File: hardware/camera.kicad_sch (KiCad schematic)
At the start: 4 parts, among them J1 DF37NC-30DS-0.4V_51_

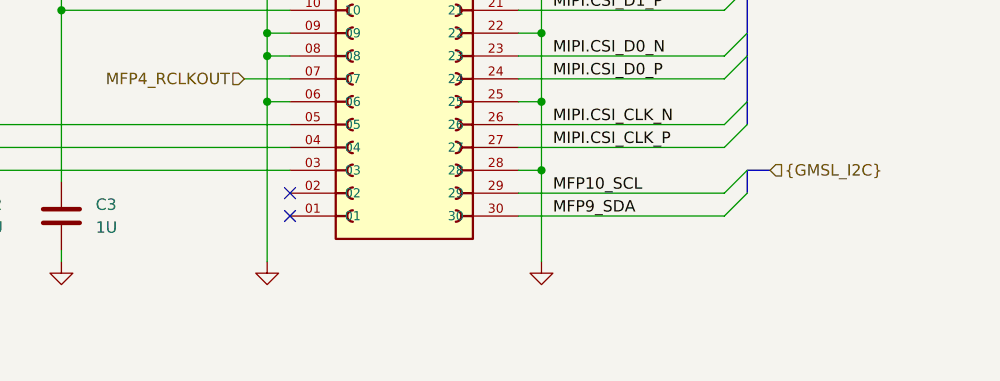
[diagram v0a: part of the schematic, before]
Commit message: finished rough pass on max96717, need cfgs. added notes to imx219 inck tolerance.
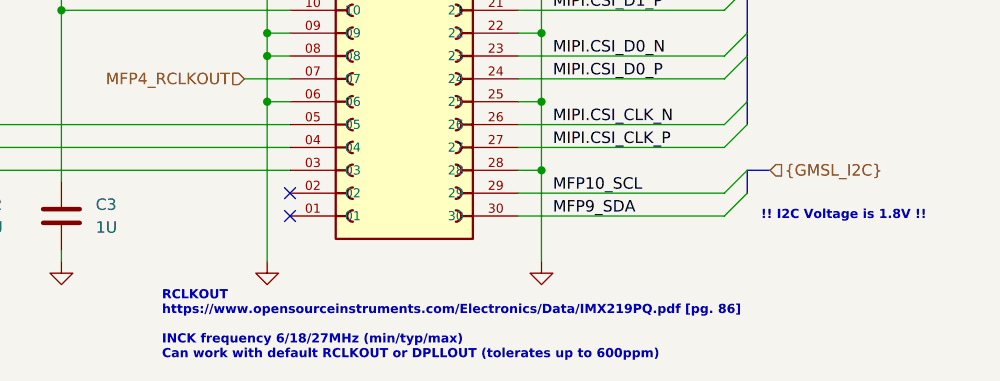
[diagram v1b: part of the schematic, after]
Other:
- note added: "!! I2C Voltage is 1.8V !!"
- note added: "RCLKOUT https://www.opensourceinstruments.com/Electronics/Data/IMX219PQ.pdf [pg. 86] INCK frequency 6/18/27MHz (min/typ/max) Can work with default RCLKOUT or DPLLOUT (tolerates up to 600ppm)"
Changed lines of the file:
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@@
+		)
+	)
+	(text "RCLKOUT\nhttps://www.opensourceinstruments.com/Electronics/Data/IMX219PQ.pdf [pg. 86]\n\nINCK frequency 6/18/27MHz (min/typ/max)\nCan work with default RCLKOUT or DPLLOUT (tolerates up to 600ppm)"
+		(exclude_from_sim no)
+		(at 119.126 126.492 0)
+		(effects
+			(font
+				(size 1.016 1.016)
+				(thickness 0.254)
+				(bold yes)
+				(color 132 132 132 1)
+			)
+			(justify left)
+		)
+	)
+	(text "!! I2C Voltage is 1.8V !!"
+		(exclude_from_sim no)
+		(at 185.674 114.3 0)
+		(effects
+			(font
+				(size 1.016 1.016)
+				(thickness 0.254)
+				(bold yes)
+				(color 255 0 0 1)
+			)
+			(justify left)
 		)
 	)
 	(label "MIPI.CSI_D3_N"
 		(at 115.57 81.28 0)
+		(fields_autoplaced yes)
 		(effects
 			(font
@@
 	(label "MIPI.CSI_D3_P"
 		(at 115.57 83.82 0)
+		(fields_autoplaced yes)
 		(effects
 			(font
@@
 	(label "MIPI.CSI_D0_P"
 		(at 162.56 99.06 0)
+		(fields_autoplaced yes)
 		(effects
 			(font
@@
 	(label "MFP10_SCL"
 		(at 162.56 111.76 0)
+		(fields_autoplaced yes)
 		(effects
 			(font
@@
 	(label "MFP9_SDA"
 		(at 162.56 114.3 0)
+		(fields_autoplaced yes)
 		(effects
 			(font
@@
 	(label "MIPI.CSI_CLK_N"
 		(at 162.56 104.14 0)
+		(fields_autoplaced yes)
 		(effects
 			(font
@@
 	(label "MIPI.CSI_D1_N"
 		(at 162.56 88.9 0)
+		(fields_autoplaced yes)
 		(effects
 			(font
@@
 	(label "MIPI.CSI_D0_N"
 		(at 162.56 96.52 0)
+		(fields_autoplaced yes)
 		(effects
 			(font
@@
 	(label "MIPI.CSI_D1_P"
 		(at 162.56 91.44 0)
+		(fields_autoplaced yes)
 		(effects
 			(font
@@
 	(label "MIPI.CSI_CLK_P"
 		(at 162.56 106.68 0)
+		(fields_autoplaced yes)
 		(effects
 			(font
@@
 	(label "MIPI.CSI_D2_N"
 		(at 162.56 81.28 0)
+		(fields_autoplaced yes)
 		(effects
 			(font
@@
 	(label "MIPI.CSI_D2_P"
 		(at 162.56 83.82 0)
+		(fields_autoplaced yes)
 		(effects
 			(font

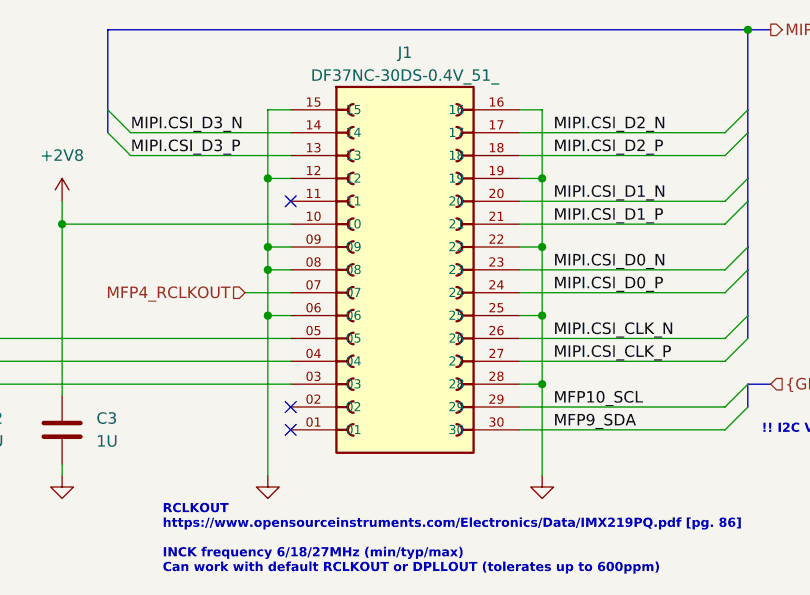
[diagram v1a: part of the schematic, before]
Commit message: Removed DF37 connector
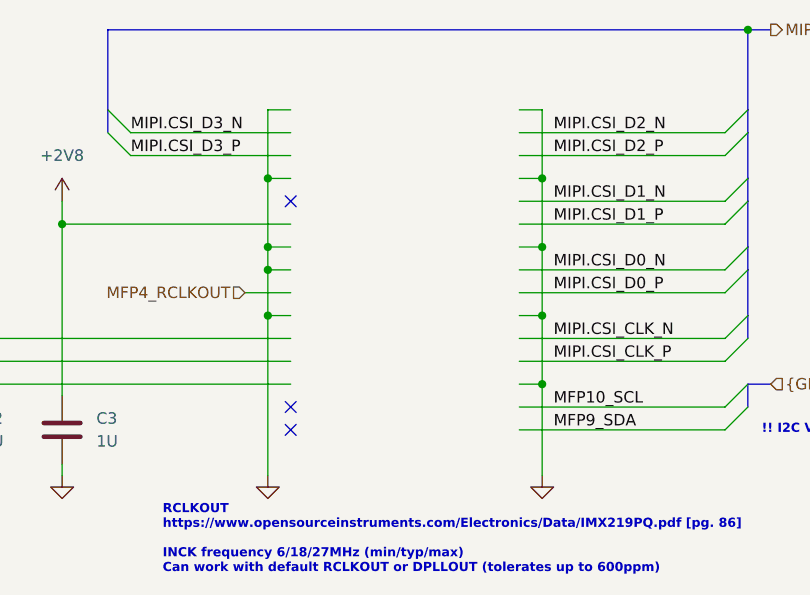
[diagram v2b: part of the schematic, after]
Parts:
- removed J1: DF37NC-30DS-0.4V_51_, user:HRS_DF37NC-30DS-0.4V_51_, symbol user:DF37NC-30DS-0.4V_51_
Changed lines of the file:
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@@
-	)
-	(symbol
-		(lib_id "user:DF37NC-30DS-0.4V_51_")
-		(at 146.05 96.52 0)
-		(unit 1)
-		(exclude_from_sim no)
-		(in_bom yes)
-		(on_board yes)
-		(dnp no)
-		(property "Reference" "J1"
-			(at 146.05 72.39 0)
-			(effects
-				(font
-					(size 1.27 1.27)
-				)
-			)
-		)
-		(property "Value" "DF37NC-30DS-0.4V_51_"
-			(at 146.05 74.93 0)
-			(effects
-				(font
-					(size 1.27 1.27)
-				)
-			)
-		)
-		(property "Footprint" "user:HRS_DF37NC-30DS-0.4V_51_"
-			(at 146.304 128.27 0)
-			(effects
-				(font
-					(size 1.27 1.27)
-				)
-				(justify bottom)
-				(hide yes)
-			)
-		)
-		(property "Datasheet" ""
-			(at 146.05 96.52 0)
-			(effects
-				(font
-					(size 1.27 1.27)
-				)
-				(hide yes)
-			)
-		)
-		(property "Description" ""
-			(at 146.05 96.52 0)
-			(effects
-				(font
-					(size 1.27 1.27)
-				)
-				(hide yes)
-			)
-		)
-		(property "PARTREV" "11.02.09"
-			(at 146.304 125.73 0)
-			(effects
-				(font
-					(size 1.27 1.27)
-				)
-				(justify bottom)
-				(hide yes)
-			)
-		)
-		(property "STANDARD" "Manufacturer Recommendations"
-			(at 146.304 130.556 0)
-			(effects
-				(font
-					(size 1.27 1.27)
-				)
-				(justify bottom)
-				(hide yes)
-			)
-		)
-		(property "MAXIMUM_PACKAGE_HEIGHT" "1.08mm"
-			(at 147.574 133.35 0)
-			(effects
-				(font
-					(size 1.27 1.27)
-				)
-				(justify bottom)
-				(hide yes)
-			)
-		)
-		(property "MANUFACTURER" "Hirose"
-			(at 139.192 133.35 0)
-			(effects
-				(font
-					(size 1.27 1.27)
-				)
-				(justify bottom)
-				(hide yes)
-			)
-		)
-		(pin "25"
-		)
-		(pin "13"
-		)
-		(pin "05"
-		)
-		(pin "17"
-		)
-		(pin "20"
-		)
-		(pin "02"
-		)
-		(pin "12"
-		)
-		(pin "10"
-		)
-		(pin "23"
-		)
-		(pin "14"
-		)
-		(pin "04"
-		)
-		(pin "15"
-		)
-		(pin "27"
-		)
-		(pin "01"
-		)
-		(pin "11"
-		)
-		(pin "21"
-		)
-		(pin "29"
-		)
-		(pin "22"
-		)
-		(pin "24"
-		)
-		(pin "30"
-		)
-		(pin "16"
-		)
-		(pin "19"
-		)
-		(pin "28"
-		)
-		(pin "26"
-		)
-		(pin "09"
-		)
-		(pin "08"
-		)
-		(pin "18"
-		)
-		(pin "06"
-		)
-		(pin "07"
-		)
-		(pin "03"
-		)
-		(instances
-			(project "minimax"
-				(path "/d9b03904-3e0d-40cc-bc70-bbd63756773a/b4a9c74b-3e83-441e-9048-ec6149d222c3"
-					(reference "J1")
-					(unit 1)
-				)
-			)
-		)
 	)
 	(symbol

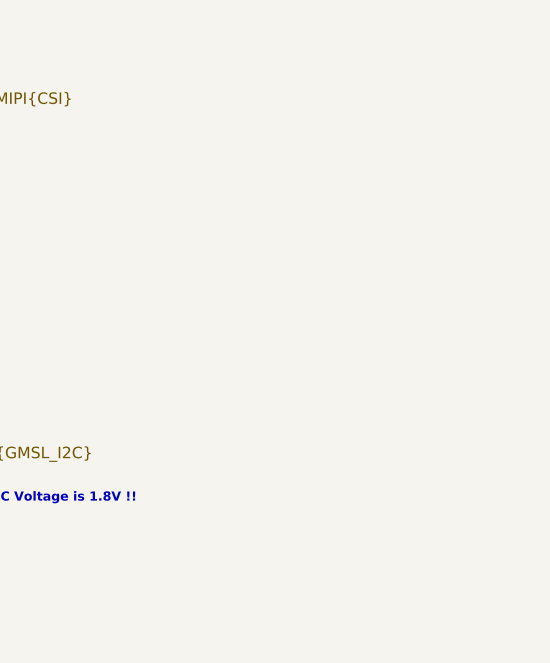
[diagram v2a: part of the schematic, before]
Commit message: added 22-pin 524352271, need to change fakra to smt
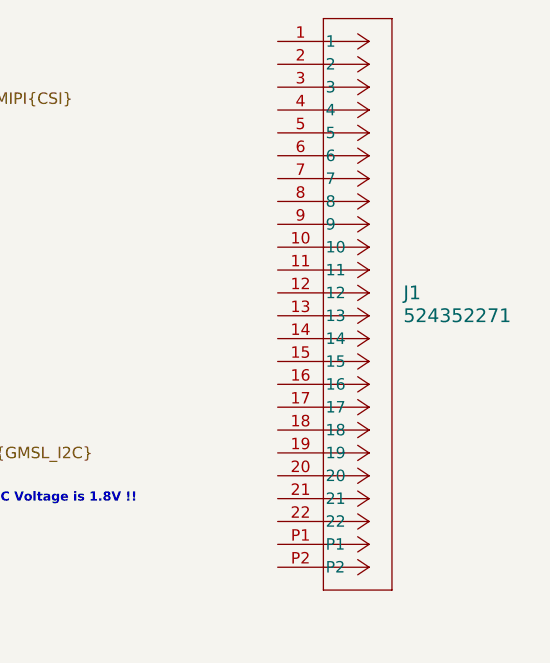
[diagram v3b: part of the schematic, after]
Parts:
- added J1: 524352271, user:CON_524352271_MOL, symbol user:524352271
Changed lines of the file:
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@@
+	)
+	(symbol
+		(lib_id "user:524352271")
+		(at 219.71 63.5 0)
+		(unit 1)
+		(exclude_from_sim no)
+		(in_bom yes)
+		(on_board yes)
+		(dnp no)
+		(fields_autoplaced yes)
+		(property "Reference" "J1"
+			(at 233.68 91.4399 0)
+			(effects
+				(font
+					(size 1.524 1.524)
+				)
+				(justify left)
+			)
+		)
+		(property "Value" "524352271"
+			(at 233.68 93.9799 0)
+			(effects
+				(font
+					(size 1.524 1.524)
+				)
+				(justify left)
+			)
+		)
+		(property "Footprint" "user:CON_524352271_MOL"
+			(at 219.71 63.5 0)
+			(effects
+				(font
+					(size 1.27 1.27)
+					(italic yes)
+				)
+				(hide yes)
+			)
+		)
+		(property "Datasheet" "524352271"
+			(at 219.71 63.5 0)
+			(effects
+				(font
+					(size 1.27 1.27)
+					(italic yes)
+				)
+				(hide yes)
+			)
+		)
+		(property "Description" ""
+			(at 219.71 63.5 0)
+			(effects
+				(font
+					(size 1.27 1.27)
+				)
+				(hide yes)
+			)
+		)
+		(pin "16"
+		)
+		(pin "10"
+		)
+		(pin "6"
+		)
+		(pin "P1"
+		)
+		(pin "2"
+		)
+		(pin "22"
+		)
+		(pin "21"
+		)
+		(pin "12"
+		)
+		(pin "11"
+		)
+		(pin "3"
+		)
+		(pin "1"
+		)
+		(pin "19"
+		)
+		(pin "20"
+		)
+		(pin "4"
+		)
+		(pin "17"
+		)
+		(pin "7"
+		)
+		(pin "8"
+		)
+		(pin "13"
+		)
+		(pin "15"
+		)
+		(pin "18"
+		)
+		(pin "14"
+		)
+		(pin "5"
+		)
+		(pin "9"
+		)
+		(pin "P2"
+		)
+		(instances
+			(project ""
+				(path "/d9b03904-3e0d-40cc-bc70-bbd63756773a/b4a9c74b-3e83-441e-9048-ec6149d222c3"
+					(reference "J1")
+					(unit 1)
+				)
+			)
+		)
 	)
 	(symbol

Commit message: cleaned up schematics
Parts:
- removed C1, C2, C3: 1U, Capacitor_SMD:C_0402_1005Metric, symbol Device:C
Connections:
- net GND: now also J1.1, J1.10, J1.13, J1.16, J1.19, J1.4, J1.7, J1.P1, J1.P2
- net MFP10_SCL: now also J1.20
- net MFP9_SDA: now also J1.21
- net MIPI.CSI_CLK_N: now also J1.8
- net MIPI.CSI_CLK_P: now also J1.9
- net MIPI.CSI_D0_N: now also J1.2
- net MIPI.CSI_D0_P: now also J1.3
- net MIPI.CSI_D1_N: now also J1.5
- net MIPI.CSI_D1_P: now also J1.6
- net MIPI.CSI_D2_N: now also J1.11
- net MIPI.CSI_D2_P: now also J1.12
- net MIPI.CSI_D3_N: now also J1.14
- net MIPI.CSI_D3_P: now also J1.15
- net POWER_EN: now reaches J1.17
- net LED_EN: now reaches J1.18
- net +3.3V: now reaches J1.22
- no-connect marks 3 -> 0
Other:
- note removed: "!! I2C Voltage is 1.8V !!"
- note removed: "RCLKOUT https://www.opensourceinstruments.com/Electronics/Data/IMX219PQ.pdf [pg. 86] INCK frequency 6/18/27MHz (min/typ/max) Can work with default RCLKOUT or DPLLOUT (tolerates up to 600ppm)"
- moved on the sheet: J1

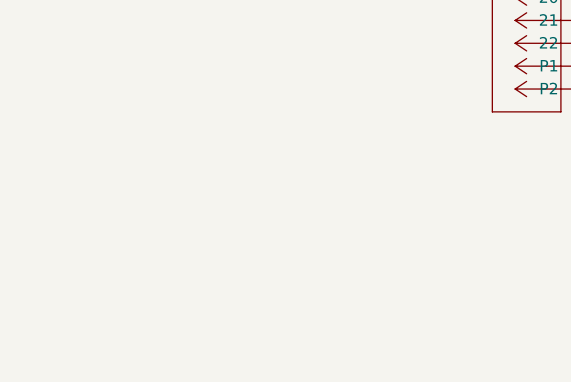
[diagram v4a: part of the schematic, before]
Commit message: started power, added smt fakra
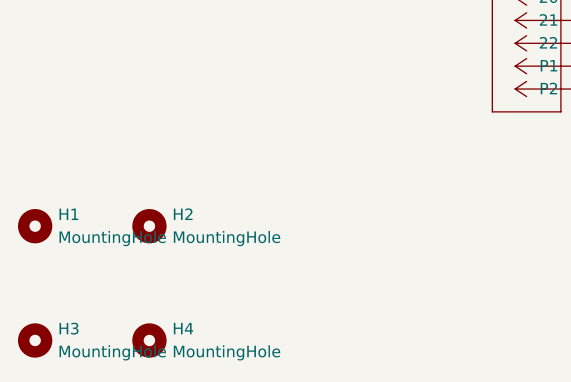
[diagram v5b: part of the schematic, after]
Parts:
- added H1, H2, H3, H4: MountingHole, MountingHole:MountingHole_2.2mm_M2, symbol Mechanical:MountingHole

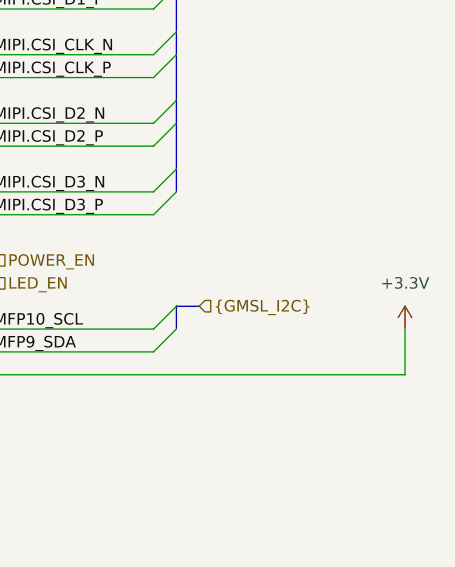
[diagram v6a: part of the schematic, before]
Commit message: cleaned up power supply and started minor power plane routing
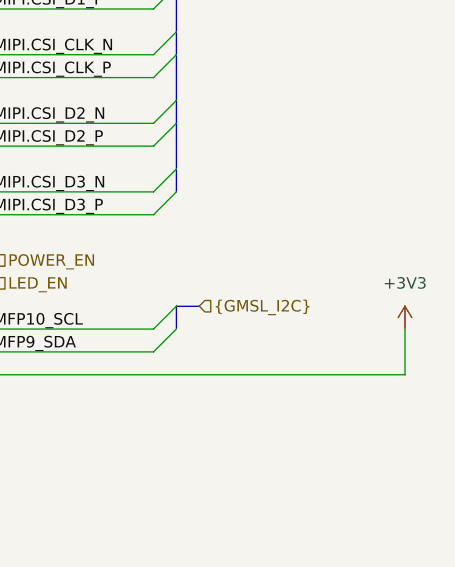
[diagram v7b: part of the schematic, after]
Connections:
- net +3.3V renamed +3V3
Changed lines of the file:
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@@
 			)
 		)
-		(property "Value" "+3.3V"
+		(property "Value" "+3V3"
 			(at 190.5 96.52 0)
 			(effects
